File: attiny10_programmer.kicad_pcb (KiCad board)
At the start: 2 copper layers, 17.8 x 30.5 mm, 12 parts, among them J1 Conn_01x03, J2 AVR-ISP-6, Q1 Q_PNP_EBC, U1 SFH617A-1, U2 ATtiny10-TS

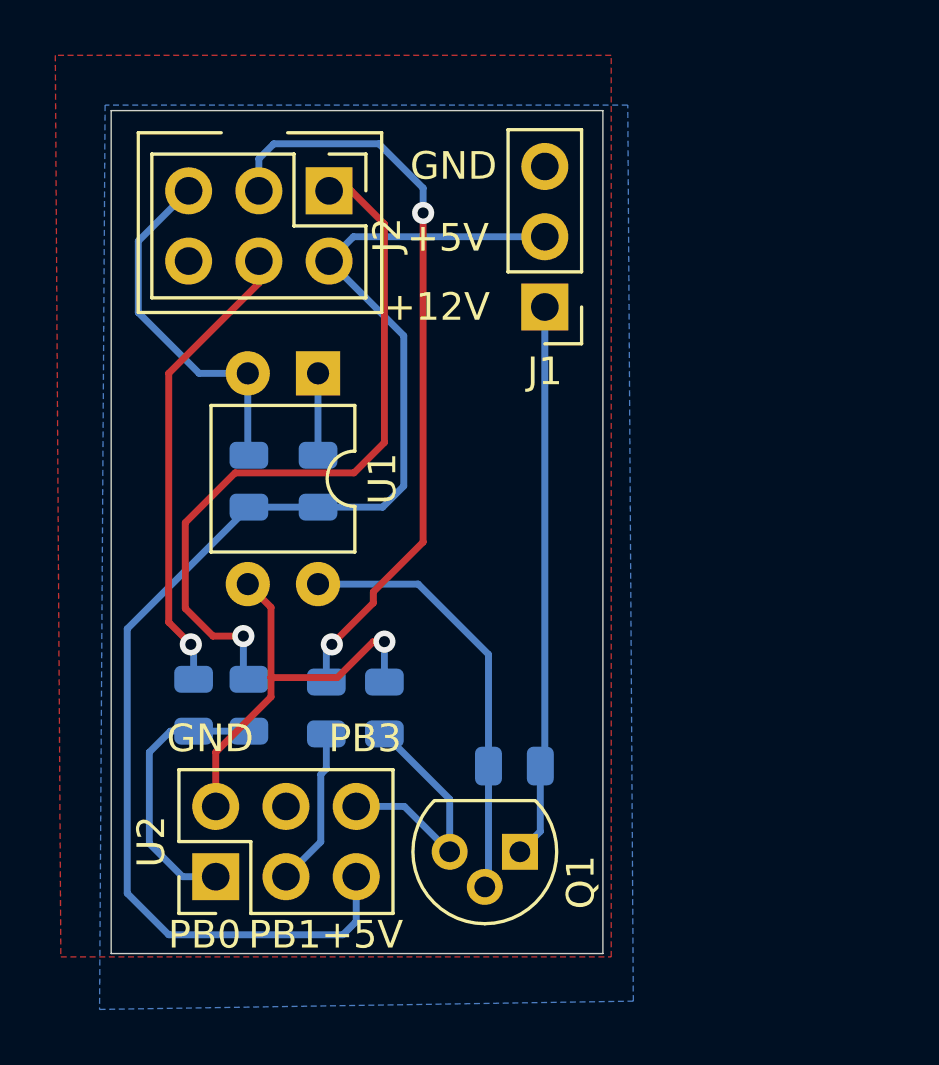
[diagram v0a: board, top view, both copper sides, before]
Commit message: Add current limiting resistor on +12v
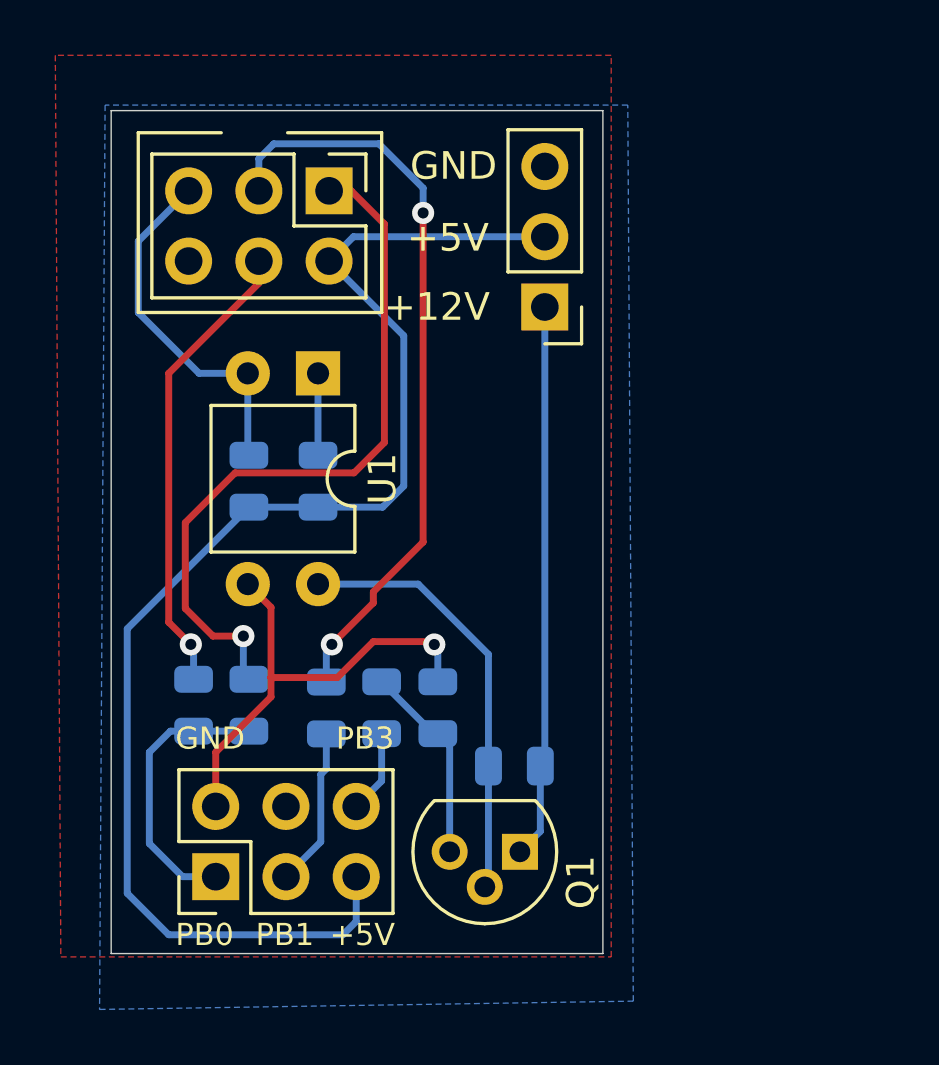
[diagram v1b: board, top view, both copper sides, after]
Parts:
- added R8: 1kR, Resistor_SMD:R_0805_2012Metric, B.Cu at (169.8, 110.5)
- moved R7 1.93 mm to (171.8, 110.5)
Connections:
- U2 pad 6: Net-(Q1-Pad3) -> Net-(R8-Pad1)
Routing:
- net Net-(R8-Pad1): track 0.00 -> 3.01 mm
- net Net-(Q1-Pad3): track 9.30 -> 7.26 mm
- net GND: track 15.3 -> 17.1 mm
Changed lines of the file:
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@@
     (thickness 1.6)
     (drawings 17)
-    (tracks 85)
+    (tracks 89)
     (zones 0)
-    (modules 12)
-    (nets 14)
+    (modules 13)
+    (nets 15)
   )
   (page A4)
@@
   )
   (setup
-    (last_trace_width 0.2)
+    (last_trace_width 0.25)
     (user_trace_width 0.2)
     (trace_clearance 0.2)
@@
     (solder_mask_min_width 0.25)
     (aux_axis_origin 0 0)
-    (visible_elements FFFFFF7F)
+    (visible_elements 7FFFFFFF)
     (pcbplotparams
       (layerselection 0x010fc_ffffffff)
@@
   (net 12 "Net-(R5-Pad1)")
   (net 13 "Net-(U2-Pad4)")
+  (net 14 "Net-(R8-Pad1)")
   (net_class Default "This is the default net class."
     (clearance 0.2)
@@
     (add_net "Net-(R2-Pad1)")
     (add_net "Net-(R5-Pad1)")
+    (add_net "Net-(R8-Pad1)")
     (add_net "Net-(U2-Pad4)")
+  )
+  (module Resistor_SMD:R_0805_2012Metric (layer B.Cu)
+    (at 169.799 110.49 90)
+    (descr "Resistor SMD 0805 (2012 Metric), square (rectangular) end terminal, IPC_7351 nominal, (Body size source: https://docs.google.com/spreadsheets/d/1BsfQQcO9C6DZCsRaXUlFlo91Tg2WpOkGARC1WS5S8t0/edit?usp=sharing), generated with kicad-footprint-generator")
+    (tags resistor)
+    (attr smd)
+    (fp_text reference R8 (at 2.667 0 270) (layer B.SilkS)
+      (effects (font (size 1 1) (thickness 0.15)) (justify mirror))
+    )
+    (fp_text value 1kR (at 0 -1.65 270) (layer B.Fab)
+      (effects (font (size 1 1) (thickness 0.15)) (justify mirror))
+    )
+    (fp_text user %R (at 0 0 270) (layer B.Fab)
+      (effects (font (size 0.5 0.5) (thickness 0.08)) (justify mirror))
+    )
+    (fp_line (start 1.68 -0.95) (end -1.68 -0.95) (layer B.CrtYd) (width 0.05))
+    (fp_line (start 1.68 0.95) (end 1.68 -0.95) (layer B.CrtYd) (width 0.05))
+    (fp_line (start -1.68 0.95) (end 1.68 0.95) (layer B.CrtYd) (width 0.05))
+    (fp_line (start -1.68 -0.95) (end -1.68 0.95) (layer B.CrtYd) (width 0.05))
+    (fp_line (start -0.258578 -0.71) (end 0.258578 -0.71) (layer B.SilkS) (width 0.12))
+    (fp_line (start -0.258578 0.71) (end 0.258578 0.71) (layer B.SilkS) (width 0.12))
+    (fp_line (start 1 -0.6) (end -1 -0.6) (layer B.Fab) (width 0.1))
+    (fp_line (start 1 0.6) (end 1 -0.6) (layer B.Fab) (width 0.1))
+    (fp_line (start -1 0.6) (end 1 0.6) (layer B.Fab) (width 0.1))
+    (fp_line (start -1 -0.6) (end -1 0.6) (layer B.Fab) (width 0.1))
+    (pad 2 smd roundrect (at 0.9375 0 90) (size 0.975 1.4) (layers B.Cu B.Paste B.Mask) (roundrect_rratio 0.25)
+      (net 8 "Net-(Q1-Pad3)"))
+    (pad 1 smd roundrect (at -0.9375 0 90) (size 0.975 1.4) (layers B.Cu B.Paste B.Mask) (roundrect_rratio 0.25)
+      (net 14 "Net-(R8-Pad1)"))
+    (model ${KISYS3DMOD}/Resistor_SMD.3dshapes/R_0805_2012Metric.wrl
+      (at (xyz 0 0 0))
+      (scale (xyz 1 1 1))
+      (rotate (xyz 0 0 0))
+    )
   )
   (module Resistor_SMD:R_0805_2012Metric (layer B.Cu)
@@
     (descr "Through hole straight pin header, 2x03, 2.54mm pitch, double rows")
     (tags "Through hole pin header THT 2x03 2.54mm double row")
-    (fp_text reference U2 (at 1.27 -2.33 90) (layer F.SilkS)
+    (fp_text reference U2 (at 1.27 -2.33 90) (layer F.SilkS) hide
       (effects (font (size 1 1) (thickness 0.15)))
     )
@@
     (fp_line (start 0 -1.27) (end 3.81 -1.27) (layer F.Fab) (width 0.1))
     (pad 6 thru_hole oval (at 2.54 5.08 90) (size 1.7 1.7) (drill 1) (layers *.Cu *.Mask)
-      (net 8 "Net-(Q1-Pad3)"))
+      (net 14 "Net-(R8-Pad1)"))
     (pad 5 thru_hole oval (at 0 5.08 90) (size 1.7 1.7) (drill 1) (layers *.Cu *.Mask)
       (net 2 +5V))
@@
   )
   (module Resistor_SMD:R_0805_2012Metric (layer B.Cu)
-    (at 169.9 110.5 270)
+    (at 171.831 110.49 270)
     (descr "Resistor SMD 0805 (2012 Metric), square (rectangular) end terminal, IPC_7351 nominal, (Body size source: https://docs.google.com/spreadsheets/d/1BsfQQcO9C6DZCsRaXUlFlo91Tg2WpOkGARC1WS5S8t0/edit?usp=sharing), generated with kicad-footprint-generator")
     (tags resistor)
     (attr smd)
-    (fp_text reference R7 (at -2.6 -1.1 270) (layer B.SilkS)
+    (fp_text reference R7 (at -2.667 -1.016 270) (layer B.SilkS)
       (effects (font (size 1 1) (thickness 0.15)) (justify mirror))
     )
@@
     (tags resistor)
     (attr smd)
-    (fp_text reference R3 (at 0.3 -1.6 90) (layer B.SilkS)
+    (fp_text reference R3 (at 2.577 -1.075 90) (layer B.SilkS)
       (effects (font (size 1 1) (thickness 0.15)) (justify mirror))
     )
@@
     (descr "Through hole straight pin header, 2x03, 2.54mm pitch, double rows")
     (tags "Through hole pin header THT 2x03 2.54mm double row")
-    (fp_text reference J2 (at 1.6 -2.1 270) (layer F.SilkS)
+    (fp_text reference J2 (at 1.6 -2.1 270) (layer F.SilkS) hide
       (effects (font (size 1 1) (thickness 0.15)))
     )
@@
     (descr "Through hole straight pin header, 1x03, 2.54mm pitch, single row")
     (tags "Through hole pin header THT 1x03 2.54mm single row")
-    (fp_text reference J1 (at 0 -2.33) (layer F.SilkS)
+    (fp_text reference J1 (at 0 -2.33) (layer F.SilkS) hide
       (effects (font (size 1 1) (thickness 0.15)))
     )
@@
   (gr_line (start 164 89.7) (end 161 89.7) (layer F.SilkS) (width 0.12))
   (gr_text PB3 (at 169.2 111.6) (layer F.SilkS)
-    (effects (font (size 1 1) (thickness 0.15)))
+    (effects (font (size 0.8 0.8) (thickness 0.12)))
   )
   (gr_text GND (at 163.6 111.6) (layer F.SilkS)
-    (effects (font (size 1 1) (thickness 0.15)))
+    (effects (font (size 0.8 0.8) (thickness 0.12)))
   )
   (gr_text PB0 (at 163.4 118.7) (layer F.SilkS)
-    (effects (font (size 1 1) (thickness 0.15)))
+    (effects (font (size 0.8 0.8) (thickness 0.12)))
   )
   (gr_text PB1 (at 166.3 118.7) (layer F.SilkS)
-    (effects (font (size 1 1) (thickness 0.15)))
+    (effects (font (size 0.8 0.8) (thickness 0.12)))
   )
   (gr_text +5V (at 169.1 118.7) (layer F.SilkS)
-    (effects (font (size 1 1) (thickness 0.15)))
+    (effects (font (size 0.8 0.8) (thickness 0.12)))
   )
   (gr_text +12V (at 171.8 96) (layer F.SilkS)
@@
   (gr_line (start 160.02 119.38) (end 177.8 119.38) (layer Edge.Cuts) (width 0.05))
   (gr_line (start 160.02 88.9) (end 160.02 119.38) (layer Edge.Cuts) (width 0.05))
-  (segment (start 165.8 106.86) (end 164.96 106.02) (width 0.25) (layer F.Cu) (net 1) (status 1000000))
-  (segment (start 163.8 114.06) (end 163.8 112.1) (width 0.25) (layer F.Cu) (net 1) (status 1000000))
-  (segment (start 163.8 112.1) (end 165.8 110.1) (width 0.25) (layer F.Cu) (net 1) (status 1000000))
-  (segment (start 165.8 109.4) (end 165.8 106.86) (width 0.25) (layer F.Cu) (net 1) (status 1000000))
-  (segment (start 165.8 110.1) (end 165.8 109.4) (width 0.25) (layer F.Cu) (net 1) (status 1000000))
-  (segment (start 165.8 109.4) (end 168.2 109.4) (width 0.25) (layer F.Cu) (net 1) (status 1000000))
-  (segment (start 169.5 108.1) (end 169.9 108.1) (width 0.25) (layer F.Cu) (net 1) (status 1000000))
-  (segment (start 168.2 109.4) (end 169.5 108.1) (width 0.25) (layer F.Cu) (net 1) (status 1000000))
-  (segment (start 169.9 108.1) (end 169.9 109.5625) (width 0.25) (layer B.Cu) (net 1) (status 1000000))
-  (via (at 169.9 108.1) (size 0.8) (drill 0.4) (layers F.Cu B.Cu) (net 1))
+  (segment (start 165.8 106.86) (end 164.96 106.02) (width 0.25) (layer F.Cu) (net 1))
+  (segment (start 163.8 114.06) (end 163.8 112.1) (width 0.25) (layer F.Cu) (net 1))
+  (segment (start 163.8 112.1) (end 165.8 110.1) (width 0.25) (layer F.Cu) (net 1))
+  (segment (start 165.8 109.4) (end 165.8 106.86) (width 0.25) (layer F.Cu) (net 1))
+  (segment (start 165.8 110.1) (end 165.8 109.4) (width 0.25) (layer F.Cu) (net 1))
+  (via (at 171.704 108.204) (size 0.8) (drill 0.4) (layers F.Cu B.Cu) (net 1))
+  (segment (start 171.6 108.1) (end 171.704 108.204) (width 0.25) (layer F.Cu) (net 1))
+  (segment (start 169.5 108.1) (end 171.6 108.1) (width 0.25) (layer F.Cu) (net 1))
+  (segment (start 165.8 109.4) (end 168.2 109.4) (width 0.25) (layer F.Cu) (net 1))
+  (segment (start 168.2 109.4) (end 169.5 108.1) (width 0.25) (layer F.Cu) (net 1))
+  (segment (start 171.831 108.331) (end 171.704 108.204) (width 0.25) (layer B.Cu) (net 1))
+  (segment (start 171.831 109.5525) (end 171.831 108.331) (width 0.25) (layer B.Cu) (net 1))
   (segment (start 165 103.2375) (end 167.5 103.2375) (width 0.25) (layer B.Cu) (net 2))
   (segment (start 168.78 93.46) (end 167.9 94.34) (width 0.25) (layer B.Cu) (net 2))
@@
   (segment (start 164.8 109.2625) (end 165 109.4625) (width 0.25) (layer B.Cu) (net 7))
   (segment (start 164.8 107.9) (end 164.8 109.2625) (width 0.25) (layer B.Cu) (net 7))
-  (segment (start 172.26 113.7975) (end 169.9 111.4375) (width 0.25) (layer B.Cu) (net 8))
-  (segment (start 172.26 115.7) (end 172.26 113.7975) (width 0.25) (layer B.Cu) (net 8))
-  (segment (start 170.62 114.06) (end 172.26 115.7) (width 0.25) (layer B.Cu) (net 8))
-  (segment (start 168.88 114.06) (end 170.62 114.06) (width 0.25) (layer B.Cu) (net 8))
+  (segment (start 172.26 111.8565) (end 171.831 111.4275) (width 0.25) (layer B.Cu) (net 8))
+  (segment (start 172.26 115.7) (end 172.26 111.8565) (width 0.25) (layer B.Cu) (net 8))
+  (segment (start 171.674 111.4275) (end 169.799 109.5525) (width 0.25) (layer B.Cu) (net 8))
+  (segment (start 171.831 111.4275) (end 171.674 111.4275) (width 0.25) (layer B.Cu) (net 8))
   (segment (start 167.5 106.02) (end 171.12 106.02) (width 0.25) (layer B.Cu) (net 9))
   (segment (start 173.6625 108.5625) (end 173.6625 112.6) (width 0.25) (layer B.Cu) (net 9))
@@
   (segment (start 167.6 115.34) (end 166.34 116.6) (width 0.25) (layer B.Cu) (net 12))
   (segment (start 167.6 112.9) (end 167.6 115.34) (width 0.25) (layer B.Cu) (net 12))
+  (segment (start 169.799 113.141) (end 168.88 114.06) (width 0.25) (layer B.Cu) (net 14))
+  (segment (start 169.799 111.4275) (end 169.799 113.141) (width 0.25) (layer B.Cu) (net 14))
   (zone (net 1) (net_name GND) (layer F.Cu) (hatch edge 0.508)
     (connect_pads (clearance 0.508))

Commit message: Add byline
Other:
- board text added: "11/17/19 WM v1.0.0"
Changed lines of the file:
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@@
   (general
     (thickness 1.6)
-    (drawings 17)
+    (drawings 18)
     (tracks 89)
     (zones 0)
@@
     )
   )
+  (gr_text "11/17/19\nWM v1.0.0" (at 175.768 104.267 90) (layer F.SilkS)
+    (effects (font (size 1 1) (thickness 0.15)))
+  )
   (gr_line (start 169.8 89.7) (end 166.4 89.7) (layer F.SilkS) (width 0.12))

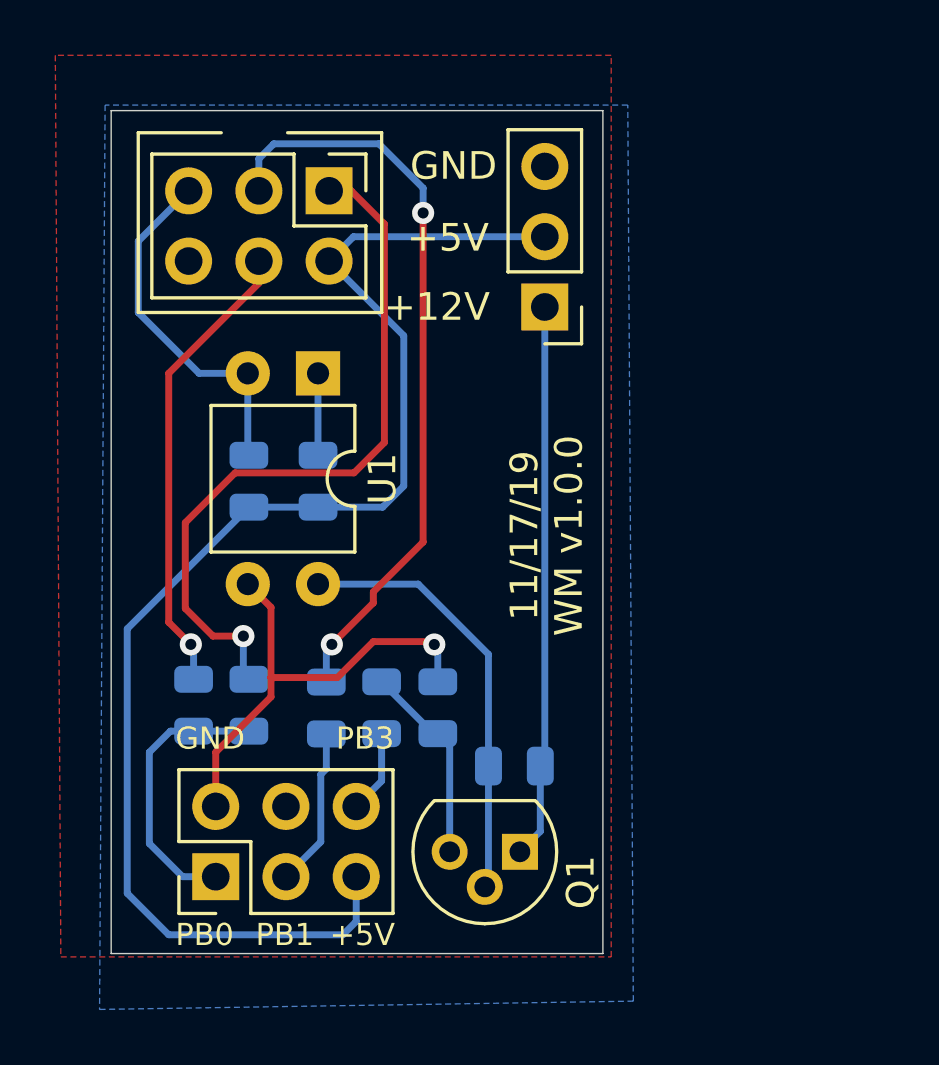
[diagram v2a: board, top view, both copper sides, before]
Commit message: Fix&Update gitignore
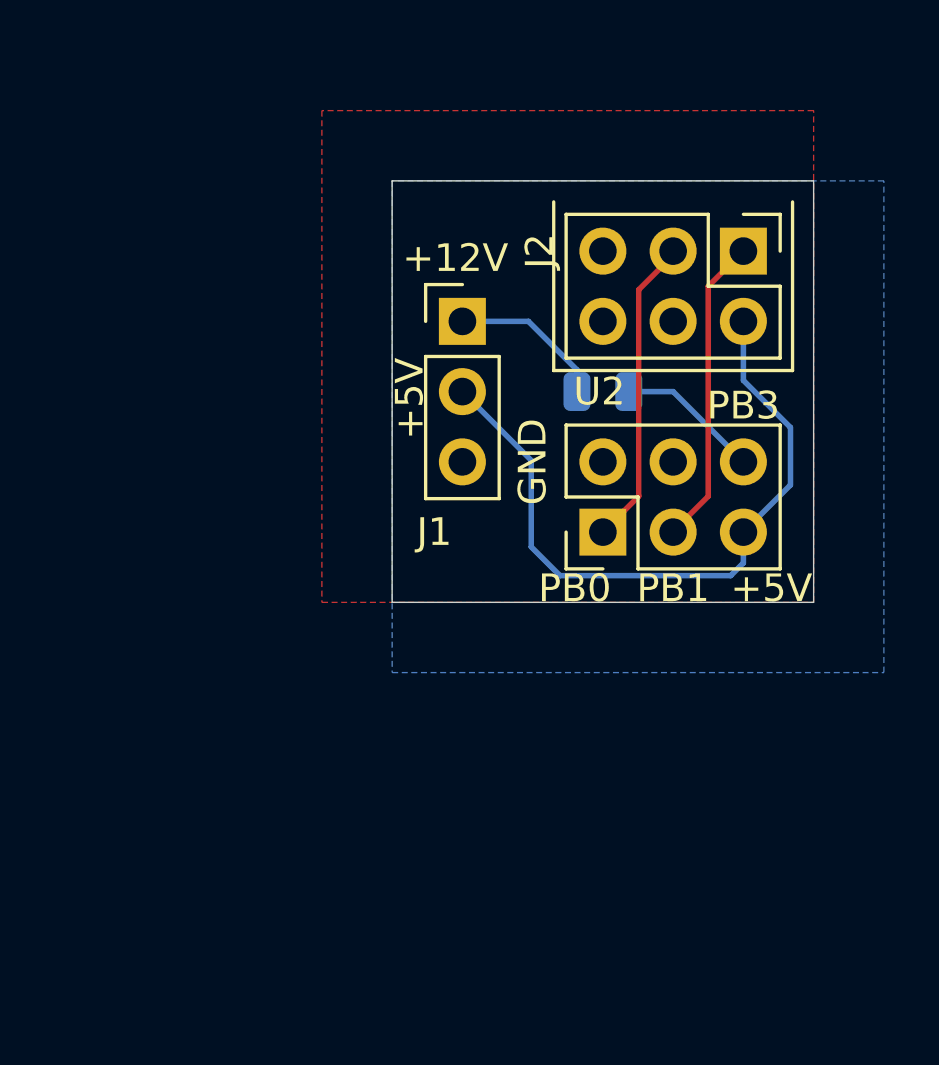
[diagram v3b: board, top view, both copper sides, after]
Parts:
- removed Q1: Q_PNP_EBC, Package_TO_SOT_THT:TO-92
- removed R2, R3, R4, R5, R6, R7: 10kR, Resistor_SMD:R_0805_2012Metric
- removed R8: 1kR, Resistor_SMD:R_0805_2012Metric
- removed U1: SFH617A-1, Package_DIP:DIP-4_W7.62mm
- R1: value 220R -> 330R
- moved U2 18.7 mm to (177.8, 104.1)
- moved J2 15.1 mm to (182.9, 94.0)
- moved R1 10.8 mm to (177.8, 99.1), turned to 180 degrees
- moved J1 3.03 mm to (172.7, 96.5), turned to 0 degrees
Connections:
- net GND renamed /GND
- J1 pad 1: +12V -> /+12V
- J1 pad 2: +5V -> /+5V
- J2 pad 2: +5V -> /+5V
- R1 pad 2: +5V -> /+12V
- U2 pad 1: Net-(R2-Pad1) -> Net-(J2-Pad3)
- U2 pad 3: Net-(R5-Pad1) -> Net-(J2-Pad1)
- U2 pad 5: +5V -> /+5V
- U2 pad 6: Net-(R8-Pad1) -> Net-(R1-Pad1)
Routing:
- net +5V: track 49.8 -> 0.00 mm
- net /+5V: track 0.00 -> 25.1 mm
- net +12V: track 20.1 -> 0.00 mm
- net /GND: track 17.1 -> 0.00 mm, vias 1 -> 0
- net Net-(J2-Pad4): track 16.8 -> 0.00 mm, vias 1 -> 0
- net Net-(J2-Pad3): track 27.3 -> 11.2 mm, vias 2 -> 0
- net Net-(Q1-Pad2): track 15.7 -> 0.00 mm
- net Net-(J2-Pad1): track 26.1 -> 11.2 mm, vias 1 -> 0
- net Net-(J2-Pad5): track 13.0 -> 0.00 mm
- net Net-(R2-Pad1): track 10.1 -> 0.00 mm
- net Net-(Q1-Pad3): track 7.26 -> 0.00 mm
- net Net-(R5-Pad1): track 5.77 -> 0.00 mm
- net /+12V: track 0.00 -> 5.65 mm
- net Net-(R8-Pad1): track 3.01 -> 0.00 mm
- net Net-(R1-Pad1): track 2.96 -> 5.19 mm
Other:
- board size 17.8 x 30.5 mm -> 15.2 x 15.2 mm
- board text removed: "11/17/19 WM v1.0.0"
